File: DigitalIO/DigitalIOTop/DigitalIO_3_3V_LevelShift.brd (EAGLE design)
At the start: 66.5 x 62.2 mm, 13 parts, among them K1 HF46105, K2 HF46105, K3 HF46105, K4 HF46105, Q1 691131710002, Q2 691131710002, Q3 691131710002, Q4 691131710002

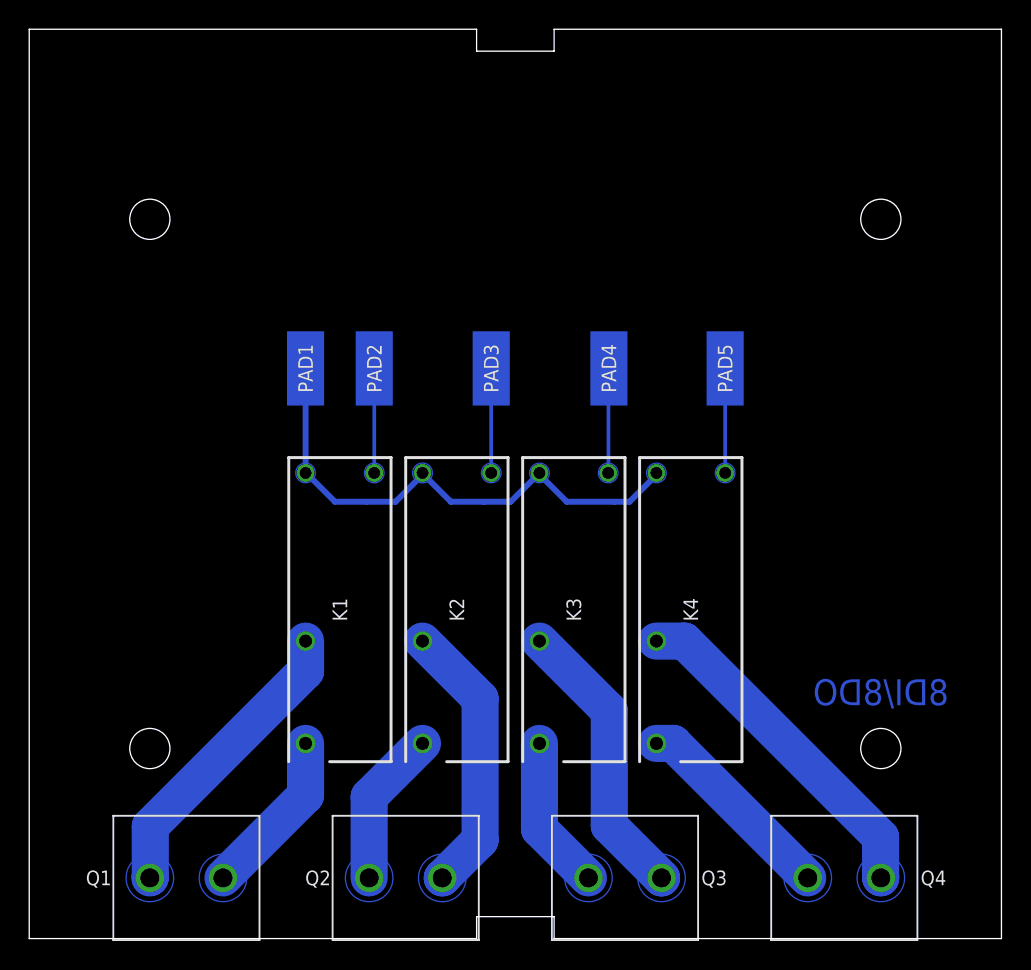
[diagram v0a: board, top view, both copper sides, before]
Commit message: Changed some drills, pads, holes, routes and headers.
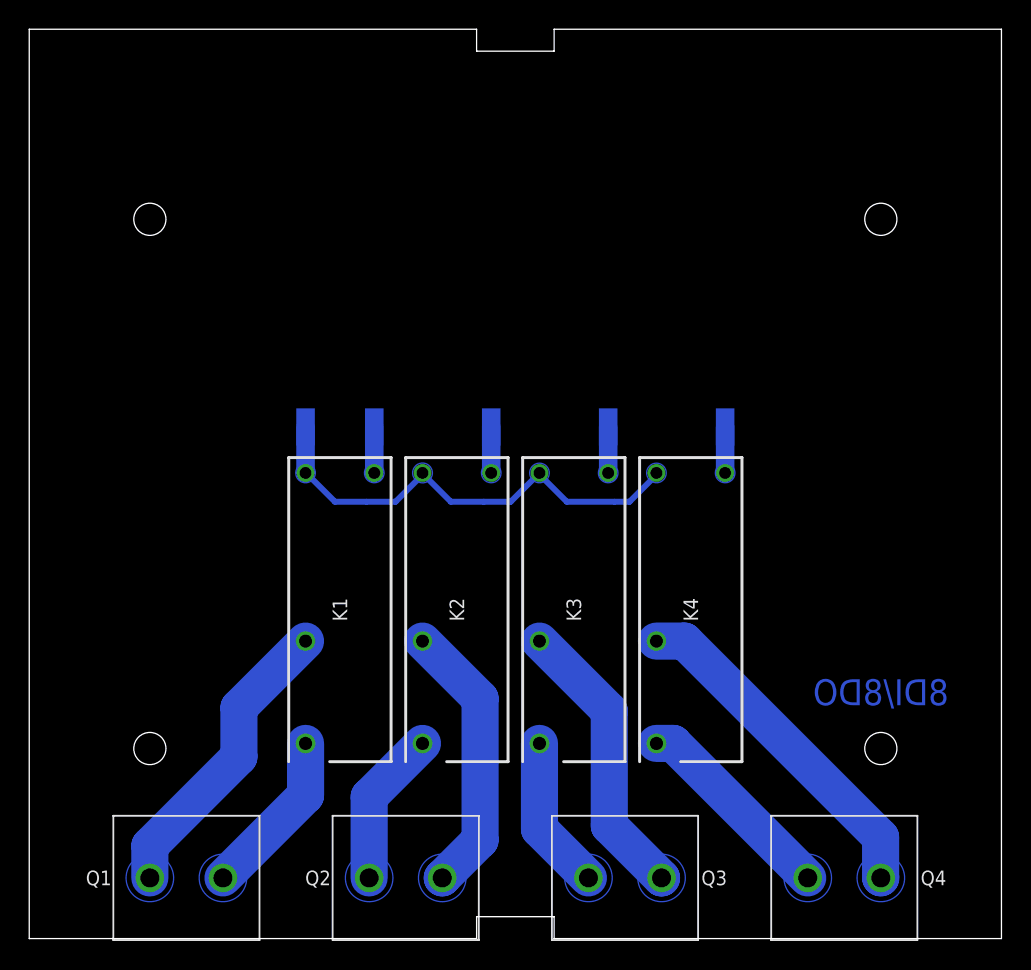
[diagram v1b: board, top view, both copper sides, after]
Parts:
- removed PAD1: +5V, wirepad:SMD2,54-5,08
- removed PAD2, PAD3, PAD4, PAD5: (no value), wirepad:SMD2,54-5,08
- added 5V, PQ1, PQ2, PQ3, PQ4: WIREPADSMD1,27-254, wirepad:SMD1,27-2,54
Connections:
- net N$1: now also 5V.1; no longer PAD1.1
- net N$14: now also PQ3.1; no longer PAD4.1
- net N$2: now also PQ2.1; no longer PAD3.1
- net N$4: now also PQ4.1; no longer PAD5.1
- net N$5: now also PQ1.1; no longer PAD2.1
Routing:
- net N$14: track 7.20 -> 3.17 mm
- net N$4: track 7.15 -> 3.15 mm
- net N$5: track 7.15 -> 3.15 mm
- net N$2: track 7.15 -> 3.16 mm
- net N$1: track 36.2 -> 32.3 mm
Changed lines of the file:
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@@
 <layer number="26" name="bNames" color="7" fill="1" visible="yes" active="yes"/>
 <layer number="27" name="tValues" color="7" fill="1" visible="no" active="yes"/>
-<layer number="28" name="bValues" color="7" fill="1" visible="yes" active="yes"/>
+<layer number="28" name="bValues" color="7" fill="1" visible="no" active="yes"/>
 <layer number="29" name="tStop" color="7" fill="3" visible="yes" active="yes"/>
-<layer number="30" name="bStop" color="7" fill="6" visible="no" active="yes"/>
+<layer number="30" name="bStop" color="7" fill="6" visible="yes" active="yes"/>
 <layer number="31" name="tCream" color="7" fill="4" visible="no" active="yes"/>
 <layer number="32" name="bCream" color="7" fill="5" visible="no" active="yes"/>
@@
 <wire x1="30.6" y1="62.2" x2="0" y2="62.2" width="0" layer="20"/>
 <wire x1="0" y1="62.2" x2="0" y2="0" width="0" layer="20"/>
-<hole x="8.25" y="49.2" drill="2.75"/>
-<hole x="58.25" y="13" drill="2.75"/>
+<hole x="8.25" y="49.2" drill="2.2"/>
+<hole x="58.25" y="13" drill="2.2"/>
 <text x="58.25" y="16.85" size="1.778" layer="16" font="vector" ratio="10" rot="MR180" align="center">8DI/8DO</text>
-<hole x="8.25" y="13" drill="2.75"/>
-<hole x="58.25" y="49.2" drill="2.75"/>
+<hole x="8.25" y="13" drill="2.2"/>
+<hole x="58.25" y="49.2" drill="2.2"/>
 <circle x="8.25" y="4.15" radius="1" width="1.6" layer="30"/>
 <circle x="13.25" y="4.15" radius="1" width="1.6" layer="30"/>
@@
 <circle x="42.9" y="31.85" radius="0.5" width="0.6" layer="30"/>
 <circle x="47.6" y="31.85" radius="0.5" width="0.6" layer="30"/>
+<circle x="8.25" y="49.2" radius="2.6" width="0" layer="30"/>
+<circle x="58.25" y="49.2" radius="2.6" width="0" layer="30"/>
+<circle x="58.25" y="13" radius="2.6" width="0" layer="30"/>
+<circle x="8.25" y="13" radius="2.6" width="0" layer="30"/>
+<circle x="8.25" y="49.2" radius="2.6" width="0" layer="29"/>
+<circle x="8.25" y="13" radius="2.6" width="0" layer="29"/>
+<circle x="58.25" y="49.2" radius="2.6" width="0" layer="29"/>
+<circle x="58.25" y="13" radius="2.6" width="0" layer="29"/>
 </plain>
 <attributes>
@@
 <attribute name="VALUE" x="43.98" y="28.85" size="1.27" layer="27" rot="R270"/>
 </element>
-<element name="PAD1" library="wirepad" package="SMD2,54-5,08" value="+5V" x="18.9" y="39" smashed="yes" rot="MR0">
-<attribute name="NAME" x="18.9" y="39" size="1" layer="25" font="vector" ratio="10" rot="R90" align="center"/>
-</element>
-<element name="PAD2" library="wirepad" package="SMD2,54-5,08" value="" x="23.6" y="39" smashed="yes" rot="MR0">
-<attribute name="VALUE" x="23.6" y="39" size="0.0254" layer="28" rot="MR0"/>
-<attribute name="NAME" x="23.6" y="39" size="1" layer="25" font="vector" ratio="10" rot="R90" align="center"/>
-</element>
-<element name="PAD3" library="wirepad" package="SMD2,54-5,08" value="" x="31.6" y="39" smashed="yes" rot="MR0">
-<attribute name="VALUE" x="31.6" y="39" size="0.0254" layer="28" rot="MR0"/>
-<attribute name="NAME" x="31.6" y="39" size="1" layer="25" font="vector" ratio="10" rot="R90" align="center"/>
-</element>
-<element name="PAD4" library="wirepad" package="SMD2,54-5,08" value="" x="39.65" y="39" smashed="yes" rot="MR0">
-<attribute name="VALUE" x="39.65" y="39" size="0.0254" layer="28" rot="MR0"/>
-<attribute name="NAME" x="39.65" y="39" size="1" layer="25" font="vector" ratio="10" rot="R90" align="center"/>
-</element>
-<element name="PAD5" library="wirepad" package="SMD2,54-5,08" value="" x="47.6" y="39" smashed="yes" rot="MR0">
-<attribute name="VALUE" x="47.6" y="39" size="0.0254" layer="28" rot="MR0"/>
-<attribute name="NAME" x="47.6" y="39" size="1" layer="25" font="vector" ratio="10" rot="R90" align="center"/>
+<element name="5V" library="wirepad" package="SMD1,27-2,54" value="WIREPADSMD1,27-254" x="18.9" y="35" smashed="yes" rot="MR0">
+<attribute name="NAME" x="18.9" y="37" size="1" layer="26" font="vector" ratio="10" rot="MR180" align="center"/>
+</element>
+<element name="PQ1" library="wirepad" package="SMD1,27-2,54" value="WIREPADSMD1,27-254" x="23.6" y="35" smashed="yes" rot="MR0">
+<attribute name="VALUE" x="23.6" y="35" size="0.0254" layer="28" rot="MR0"/>
+<attribute name="NAME" x="23.6" y="37" size="1" layer="26" font="vector" ratio="10" rot="MR180" align="center"/>
+</element>
+<element name="PQ2" library="wirepad" package="SMD1,27-2,54" value="WIREPADSMD1,27-254" x="31.6" y="35" smashed="yes" rot="MR0">
+<attribute name="VALUE" x="31.6" y="35" size="0.0254" layer="28" rot="MR0"/>
+<attribute name="NAME" x="31.6" y="37" size="1" layer="26" font="vector" ratio="10" rot="MR180" align="center"/>
+</element>
+<element name="PQ3" library="wirepad" package="SMD1,27-2,54" value="WIREPADSMD1,27-254" x="39.6" y="35" smashed="yes" rot="MR0">
+<attribute name="VALUE" x="39.6" y="35" size="0.0254" layer="28" rot="MR0"/>
+<attribute name="NAME" x="39.6" y="37" size="1" layer="26" font="vector" ratio="10" rot="MR180" align="center"/>
+</element>
+<element name="PQ4" library="wirepad" package="SMD1,27-2,54" value="WIREPADSMD1,27-254" x="47.6" y="35" smashed="yes" rot="MR0">
+<attribute name="VALUE" x="47.6" y="35" size="0.0254" layer="28" rot="MR0"/>
+<attribute name="NAME" x="47.6" y="37" size="1" layer="26" font="vector" ratio="10" rot="MR180" align="center"/>
 </element>
 <element name="Q1" library="con-wuerth" package="691131710002" value="691131710002" x="10.75" y="4.15" smashed="yes" rot="R180">
@@
 <contactref element="K4" pad="2"/>
 <contactref element="K3" pad="2"/>
-<contactref element="PAD1" pad="1"/>
+<contactref element="5V" pad="1"/>
 <contactref element="K2" pad="2"/>
-<wire x1="18.9033" y1="38.834440625" x2="18.9033" y2="31.925640625" width="0.4064" layer="16"/>
 <wire x1="18.9033" y1="31.925640625" x2="18.9" y2="31.85" width="0.254" layer="16"/>
-<wire x1="18.9033" y1="38.834440625" x2="18.9" y2="39" width="0.254" layer="16"/>
 <wire x1="28.84" y1="29.88" x2="27.02" y2="31.7" width="0.4064" layer="16"/>
 <wire x1="31.0896" y1="29.88" x2="28.84" y2="29.88" width="0.4064" layer="16"/>
@@
 <vertex x="18.42" y="32.32" curve="180"/>
 </polygon>
+<wire x1="18.9" y1="35" x2="18.9" y2="31.85" width="1.27" layer="16"/>
 </signal>
 <signal name="N$2">
 <contactref element="K2" pad="1"/>
-<contactref element="PAD3" pad="1"/>
-<wire x1="31.594640625" y1="38.8344375" x2="31.594640625" y2="31.9256375" width="0.254" layer="16"/>
+<contactref element="PQ2" pad="1"/>
 <wire x1="31.594640625" y1="31.9256375" x2="31.6" y2="31.85" width="0.254" layer="16"/>
-<wire x1="31.594640625" y1="38.8344375" x2="31.6" y2="39" width="0.254" layer="16"/>
 <polygon width="0.254" layer="16" thermals="no">
 <vertex x="32.08" y="31.38" curve="180"/>
 <vertex x="31.12" y="32.32" curve="180"/>
 </polygon>
+<wire x1="31.594640625" y1="31.9256375" x2="31.6" y2="31.9256375" width="1.27" layer="16"/>
+<wire x1="31.6" y1="31.9256375" x2="31.6" y2="35" width="1.27" layer="16"/>
 </signal>
 <signal name="N$4">
 <contactref element="K4" pad="1"/>
-<contactref element="PAD5" pad="1"/>
-<wire x1="47.600971875" y1="38.8344375" x2="47.600971875" y2="31.9256375" width="0.254" layer="16"/>
-<wire x1="47.600971875" y1="31.9256375" x2="47.6" y2="31.85" width="0.254" layer="16"/>
-<wire x1="47.600971875" y1="38.8344375" x2="47.6" y2="39" width="0.254" layer="16"/>
+<contactref element="PQ4" pad="1"/>
 <polygon width="0.254" layer="16" thermals="no">
 <vertex x="48.08" y="32.32" curve="180"/>
 <vertex x="47.12" y="31.38" curve="180"/>
 </polygon>
+<wire x1="47.6" y1="35" x2="47.6" y2="31.85" width="1.27" layer="16"/>
 </signal>
 <signal name="N$5">
 <contactref element="K1" pad="1"/>
-<contactref element="PAD2" pad="1"/>
-<wire x1="23.600134375" y1="38.880915625" x2="23.600134375" y2="31.972115625" width="0.254" layer="16"/>
-<wire x1="23.600134375" y1="31.972115625" x2="23.6" y2="31.85" width="0.254" layer="16"/>
-<wire x1="23.600134375" y1="38.880915625" x2="23.6" y2="39" width="0.254" layer="16"/>
+<contactref element="PQ1" pad="1"/>
 <polygon width="0.254" layer="16" thermals="no">
 <vertex x="24.08" y="31.38" curve="180"/>
 <vertex x="23.12" y="32.32" curve="180"/>
 </polygon>
+<wire x1="23.6" y1="35" x2="23.6" y2="31.85" width="1.27" layer="16"/>
 </signal>
 <signal name="N$6">
@@
 <contactref element="K1" pad="COM"/>
 <contactref element="Q1" pad="2"/>
-<wire x1="18.9" y1="20.35" x2="18.9" y2="18.2959375" width="2.54" layer="16"/>
-<wire x1="18.9" y1="18.2959375" x2="8.279240625" y2="7.675178125" width="2.54" layer="16"/>
-<wire x1="8.279240625" y1="7.675178125" x2="8.279240625" y2="4.179240625" width="2.54" layer="16"/>
-<wire x1="8.279240625" y1="4.179240625" x2="8.25" y2="4.15" width="2.54" layer="16"/>
 <polygon width="0.35" layer="16" thermals="no">
 <vertex x="9.35" y="5.35" curve="180"/>
 <vertex x="7.15" y="2.95" curve="180"/>
 </polygon>
+<wire x1="8.25" y1="4.15" x2="8.25" y2="6.345346875" width="2.54" layer="16"/>
+<wire x1="8.25" y1="6.345346875" x2="14.3434375" y2="12.438784375" width="2.54" layer="16"/>
+<wire x1="14.3434375" y1="12.438784375" x2="14.3434375" y2="15.7934375" width="2.54" layer="16"/>
+<wire x1="14.3434375" y1="15.7934375" x2="18.9" y2="20.35" width="2.54" layer="16"/>
 </signal>
 <signal name="N$8">
@@
 </signal>
 <signal name="N$14">
-<contactref element="PAD4" pad="1"/>
+<contactref element="PQ3" pad="1"/>
 <contactref element="K3" pad="1"/>
 <wire x1="39.6" y1="31.85" x2="39.6162625" y2="31.85" width="0.254" layer="16"/>
-<wire x1="39.6162625" y1="31.85" x2="39.6162625" y2="38.168415625" width="0.254" layer="16"/>
-<wire x1="39.6162625" y1="38.168415625" x2="39.65" y2="38.168415625" width="0.254" layer="16"/>
-<wire x1="39.65" y1="38.168415625" x2="39.65" y2="39" width="0.254" layer="16"/>
 <polygon width="0.254" layer="16" thermals="no">
 <vertex x="40.08" y="31.38" curve="180"/>
 <vertex x="39.12" y="32.32" curve="180"/>
 </polygon>
+<wire x1="39.6" y1="35" x2="39.6" y2="31.85" width="1.27" layer="16"/>
 </signal>
 </signals>

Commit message: Prepare for production.
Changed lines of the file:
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@@
 <wire x1="18.9033" y1="31.925640625" x2="18.9" y2="31.85" width="0.254" layer="16"/>
 <wire x1="28.84" y1="29.88" x2="27.02" y2="31.7" width="0.4064" layer="16"/>
-<wire x1="31.0896" y1="29.88" x2="28.84" y2="29.88" width="0.4064" layer="16"/>
-<wire x1="32.93" y1="29.88" x2="31.0896" y2="29.88" width="0.4064" layer="16"/>
+<wire x1="32.93" y1="29.88" x2="28.84" y2="29.88" width="0.4064" layer="16"/>
 <wire x1="34.75" y1="31.7" x2="32.93" y2="29.88" width="0.4064" layer="16"/>
 <wire x1="27.02" y1="31.7" x2="26.9" y2="31.85" width="0.254" layer="16"/>
 <wire x1="34.75" y1="31.7" x2="34.9" y2="31.85" width="0.254" layer="16"/>
 <wire x1="41.06" y1="29.88" x2="42.88" y2="31.7" width="0.4064" layer="16"/>
-<wire x1="40.03" y1="29.88" x2="41.06" y2="29.88" width="0.4064" layer="16"/>
-<wire x1="36.77" y1="29.88" x2="40.03" y2="29.88" width="0.4064" layer="16"/>
+<wire x1="36.77" y1="29.88" x2="41.06" y2="29.88" width="0.4064" layer="16"/>
 <wire x1="34.95" y1="31.7" x2="36.77" y2="29.88" width="0.4064" layer="16"/>
 <wire x1="42.88" y1="31.7" x2="42.9" y2="31.85" width="0.254" layer="16"/>
 <wire x1="34.95" y1="31.7" x2="34.9" y2="31.85" width="0.254" layer="16"/>
 <wire x1="20.91" y1="29.88" x2="19.1" y2="31.69" width="0.4064" layer="16"/>
-<wire x1="23.070259375" y1="29.88" x2="20.91" y2="29.88" width="0.4064" layer="16"/>
-<wire x1="25.055834375" y1="29.88" x2="23.070259375" y2="29.88" width="0.4064" layer="16"/>
+<wire x1="25.055834375" y1="29.88" x2="20.91" y2="29.88" width="0.4064" layer="16"/>
 <wire x1="26.87585" y1="31.7" x2="25.055834375" y2="29.88" width="0.4064" layer="16"/>
 <wire x1="19.1" y1="31.69" x2="18.9" y2="31.85" width="0.254" layer="16"/>

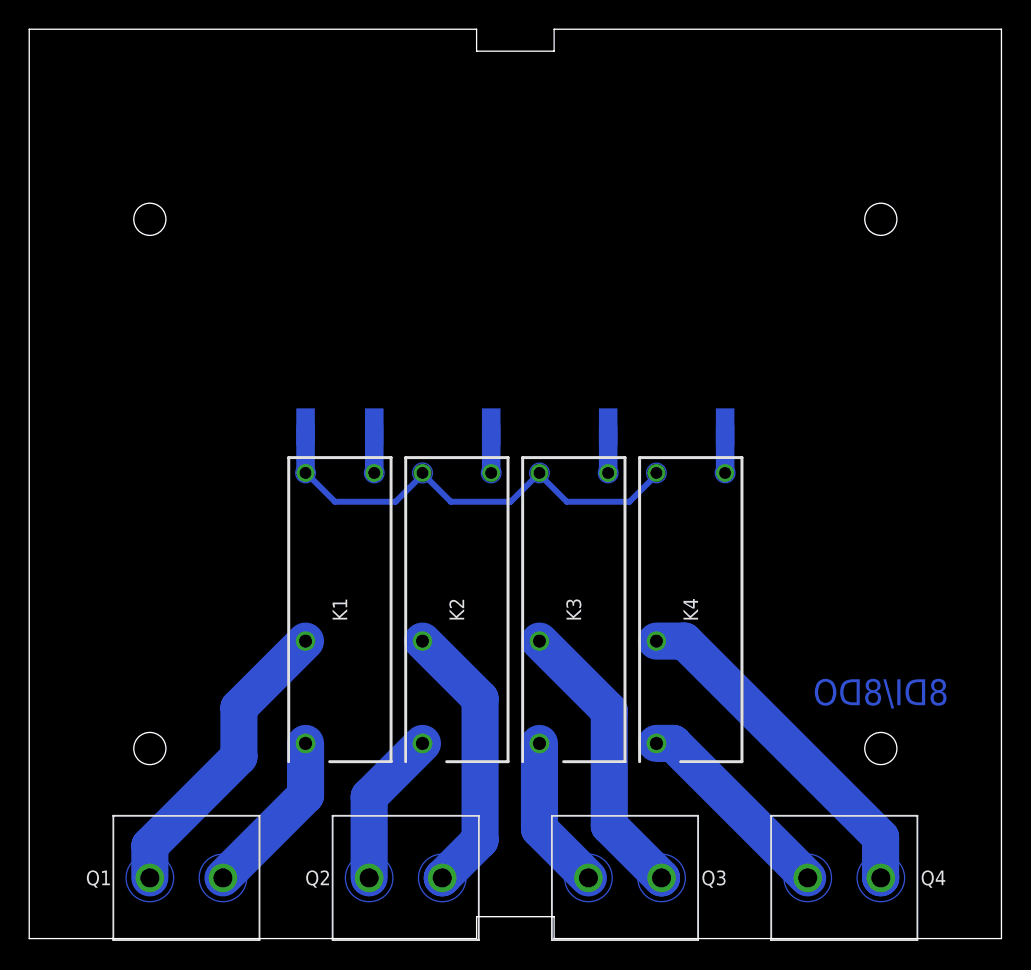
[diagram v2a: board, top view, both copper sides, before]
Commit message: Add ground plane on top pcb.
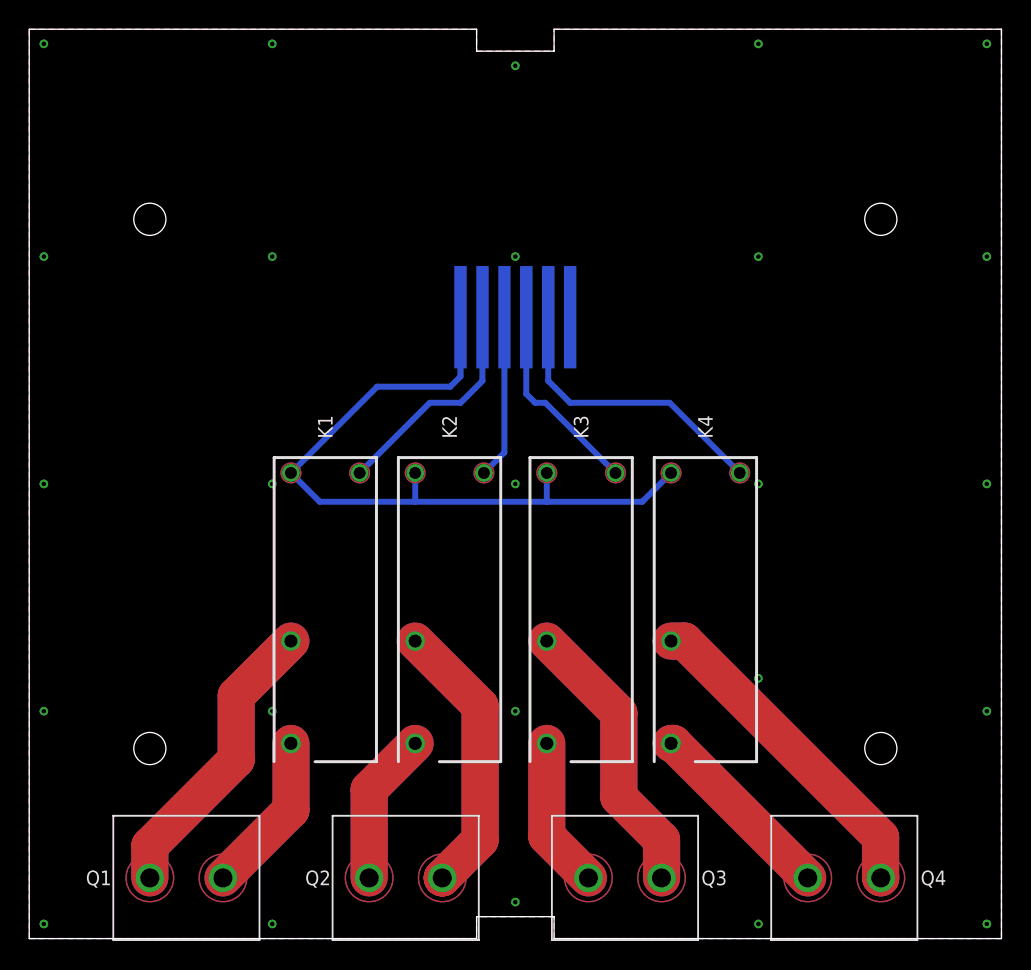
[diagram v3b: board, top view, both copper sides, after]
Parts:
- removed 5V, PQ1, PQ2, PQ3, PQ4: WIREPADSMD1,27-254, wirepad:SMD1,27-2,54
- added X1: 87438-06, con-molex:87438-06
- moved K1 1.00 mm to (20.2, 22.5)
- moved K4 1.00 mm to (46.2, 22.5)
- moved K2 0.50 mm to (28.8, 22.5)
- moved K3 0.50 mm to (37.8, 22.5)
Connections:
- removed net N$1: 5V.1, K1.2, K2.2, K3.2, K4.2
- new net +5V: K1.2, K2.2, K3.2, K4.2, X1.1
- new net GND: X1.6
- net N$14: now also X1.4; no longer PQ3.1
- net N$2: now also X1.3; no longer PQ2.1
- net N$4: now also X1.5; no longer PQ4.1
- net N$5: now also X1.2; no longer PQ1.1
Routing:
- net +5V: track 0.00 -> 50.0 mm
- net N$1: track 32.3 -> 0.00 mm
- net N$13: track 23.7 -> 45.4 mm
- net N$7: track 20.6 -> 40.4 mm
- net N$9: track 18.9 -> 38.2 mm
- net N$11: track 19.7 -> 38.9 mm
- net N$4: track 3.15 -> 20.1 mm
- net N$5: track 3.15 -> 15.4 mm
- net N$12: track 14.2 -> 26.3 mm
- net N$14: track 3.17 -> 14.1 mm
- net N$6: track 11.5 -> 22.3 mm
- net N$8: track 10.7 -> 21.0 mm
- net N$10: track 10.6 -> 20.8 mm
- net N$2: track 3.16 -> 11.2 mm
- added copper zone on layer 1, net +5V
- added copper zone on layer 16, net +5V
- added copper zone on layer 1, net GND
- added copper zone on layer 16, net GND
- added copper zone on layer 1, net N$10
- added copper zone on layer 1, net N$11
- added copper zone on layer 1, net N$12
- added copper zone on layer 1, net N$13
- added copper zone on layer 1, net N$14
- added copper zone on layer 1, net N$2
- added copper zone on layer 1, net N$4
- added copper zone on layer 1, net N$5
- added copper zone on layer 1, net N$6
- added copper zone on layer 1, net N$7
- added copper zone on layer 1, net N$8
- added copper zone on layer 1, net N$9
- removed copper zone on layer 16, net N$1
